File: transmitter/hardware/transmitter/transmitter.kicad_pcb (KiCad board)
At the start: 2 copper layers, 56 x 47 mm, 47 parts, among them J1 SOIL, J2 SOIL, J3 USB_UART, J4 PWR, J5 SOIL, J6 SOIL, J7 SOIL, J8 SOIL, Q1 Si2305CDS, Q2 BSS138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

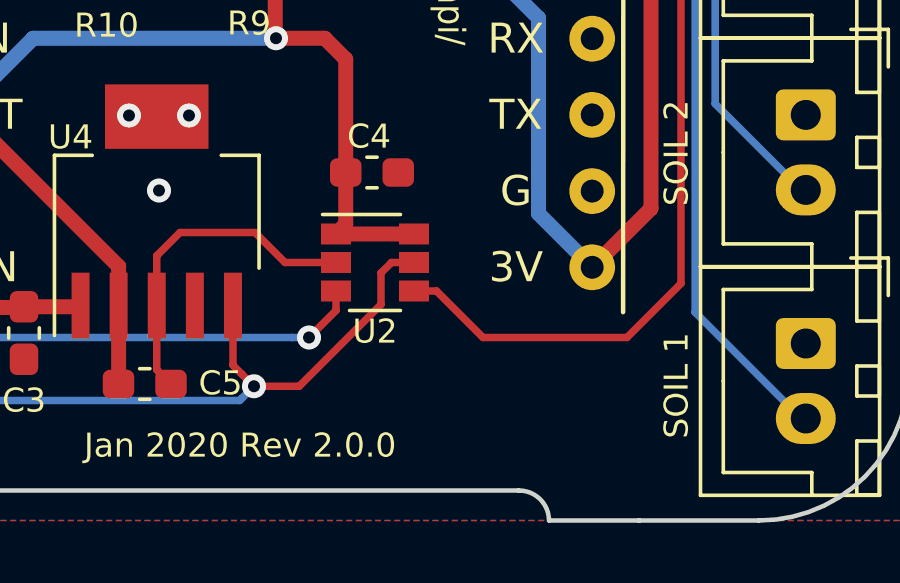
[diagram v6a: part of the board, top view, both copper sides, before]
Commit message: tpl5111 layout tweak
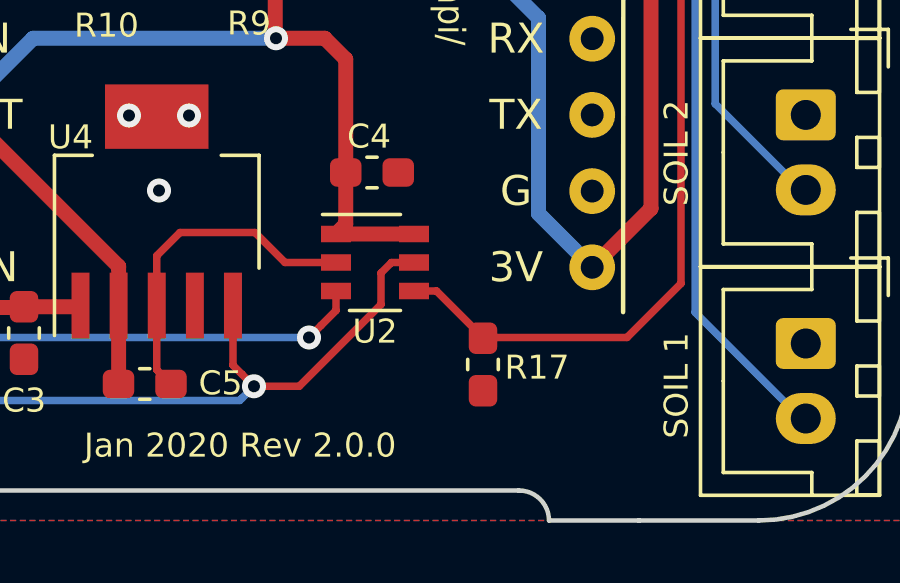
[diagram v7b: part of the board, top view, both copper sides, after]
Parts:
- added R17: 10K, Resistor_SMD:R_0603_1608Metric_Pad1.05x0.95mm_HandSolder, F.Cu at (156.4, 106.7)
- U2: footprint Package_TO_SOT_SMD:SuperSOT-6 -> tpl511x:SOT-6-DDC
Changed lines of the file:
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@@
     (tracks 295)
     (zones 0)
-    (modules 47)
+    (modules 48)
     (nets 28)
   )
@@
     (pad_drill 0.762)
     (pad_to_mask_clearance 0)
+    (solder_mask_min_width 0.25)
     (aux_axis_origin 0 0)
     (grid_origin 134.62 67.945)
@@
     (add_net "Net-(Q3-Pad3)")
   )
+  (module tpl511x:SOT-6-DDC (layer F.Cu)
+    (at 152.82 103.345)
+    (descr "6-pin SuperSOT package http://www.mouser.com/ds/2/149/FMB5551-889214.pdf")
+    (tags "SuperSOT-6 SSOT-6")
+    (attr smd)
+    (fp_text reference U2 (at 0 2.3) (layer F.SilkS)
+      (effects (font (size 0.8 0.8) (thickness 0.15)))
+    )
+    (fp_text value tpl5111 (at 0 2.5) (layer F.Fab)
+      (effects (font (size 1 1) (thickness 0.15)))
+    )
+    (fp_text user %R (at 0 0 90) (layer F.Fab)
+      (effects (font (size 0.5 0.5) (thickness 0.075)))
+    )
+    (fp_line (start 0.85 -1.6) (end -1.75 -1.6) (layer F.SilkS) (width 0.12))
+    (fp_line (start 0.85 1.6) (end -0.85 1.6) (layer F.SilkS) (width 0.12))
+    (fp_line (start -0.85 1.45) (end 0.85 1.45) (layer F.Fab) (width 0.12))
+    (fp_line (start 0.85 1.45) (end 0.85 -1.45) (layer F.Fab) (width 0.12))
+    (fp_line (start 0.85 -1.45) (end -0.4 -1.45) (layer F.Fab) (width 0.12))
+    (fp_line (start -0.4 -1.45) (end -0.85 -1) (layer F.Fab) (width 0.12))
+    (fp_line (start -0.85 -1) (end -0.85 1.45) (layer F.Fab) (width 0.12))
+    (fp_line (start -2.05 -1.7) (end 2.05 -1.7) (layer F.CrtYd) (width 0.05))
+    (fp_line (start -2.05 -1.7) (end -2.05 1.7) (layer F.CrtYd) (width 0.05))
+    (fp_line (start 2.05 1.7) (end 2.05 -1.7) (layer F.CrtYd) (width 0.05))
+    (fp_line (start 2.05 1.7) (end -2.05 1.7) (layer F.CrtYd) (width 0.05))
+    (pad 1 smd rect (at -1.3 -0.95) (size 1 0.55) (layers F.Cu F.Paste F.Mask)
+      (net 15 /VBAT))
+    (pad 2 smd rect (at -1.3 0) (size 1 0.55) (layers F.Cu F.Paste F.Mask)
+      (net 1 GND))
+    (pad 3 smd rect (at -1.3 0.95) (size 1 0.55) (layers F.Cu F.Paste F.Mask)
+      (net 25 "Net-(JP1-Pad2)"))
+    (pad 4 smd rect (at 1.3 0.95) (size 1 0.55) (layers F.Cu F.Paste F.Mask)
+      (net 22 DONE))
+    (pad 6 smd rect (at 1.3 -0.95) (size 1 0.55) (layers F.Cu F.Paste F.Mask)
+      (net 15 /VBAT))
+    (pad 5 smd rect (at 1.3 0) (size 1 0.55) (layers F.Cu F.Paste F.Mask)
+      (net 27 "Net-(TP1-Pad1)"))
+    (model ${KISYS3DMOD}/Package_TO_SOT_SMD.3dshapes/SuperSOT-6.wrl
+      (at (xyz 0 0 0))
+      (scale (xyz 1 1 1))
+      (rotate (xyz 0 0 0))
+    )
+  )
   (module "ESP8266:NodeMCU1.0(12-E)" locked (layer F.Cu)
     (at 148.59 88.9)
@@
     )
   )
-  (module Package_TO_SOT_SMD:SuperSOT-6 (layer F.Cu)
-    (at 152.82 103.345)
-    (descr "6-pin SuperSOT package http://www.mouser.com/ds/2/149/FMB5551-889214.pdf")
-    (tags "SuperSOT-6 SSOT-6")
-    (attr smd)
-    (fp_text reference U2 (at 0 2.3) (layer F.SilkS)
-      (effects (font (size 0.8 0.8) (thickness 0.15)))
-    )
-    (fp_text value tpl5111 (at 0 2.5) (layer F.Fab)
-      (effects (font (size 1 1) (thickness 0.15)))
-    )
-    (fp_text user %R (at 0 0 90) (layer F.Fab)
-      (effects (font (size 0.5 0.5) (thickness 0.075)))
-    )
-    (fp_line (start 0.85 -1.6) (end -1.75 -1.6) (layer F.SilkS) (width 0.12))
-    (fp_line (start 0.85 1.6) (end -0.85 1.6) (layer F.SilkS) (width 0.12))
-    (fp_line (start -0.85 1.45) (end 0.85 1.45) (layer F.Fab) (width 0.12))
-    (fp_line (start 0.85 1.45) (end 0.85 -1.45) (layer F.Fab) (width 0.12))
-    (fp_line (start 0.85 -1.45) (end -0.4 -1.45) (layer F.Fab) (width 0.12))
-    (fp_line (start -0.4 -1.45) (end -0.85 -1) (layer F.Fab) (width 0.12))
-    (fp_line (start -0.85 -1) (end -0.85 1.45) (layer F.Fab) (width 0.12))
-    (fp_line (start -2.05 -1.7) (end 2.05 -1.7) (layer F.CrtYd) (width 0.05))
-    (fp_line (start -2.05 -1.7) (end -2.05 1.7) (layer F.CrtYd) (width 0.05))
-    (fp_line (start 2.05 1.7) (end 2.05 -1.7) (layer F.CrtYd) (width 0.05))
-    (fp_line (start 2.05 1.7) (end -2.05 1.7) (layer F.CrtYd) (width 0.05))
-    (pad 1 smd rect (at -1.3 -0.95) (size 1 0.7) (layers F.Cu F.Paste F.Mask)
-      (net 15 /VBAT))
-    (pad 2 smd rect (at -1.3 0) (size 1 0.7) (layers F.Cu F.Paste F.Mask)
-      (net 1 GND))
-    (pad 3 smd rect (at -1.3 0.95) (size 1 0.7) (layers F.Cu F.Paste F.Mask)
-      (net 25 "Net-(JP1-Pad2)"))
-    (pad 4 smd rect (at 1.3 0.95) (size 1 0.7) (layers F.Cu F.Paste F.Mask)
-      (net 22 DONE))
-    (pad 6 smd rect (at 1.3 -0.95) (size 1 0.7) (layers F.Cu F.Paste F.Mask)
-      (net 15 /VBAT))
-    (pad 5 smd rect (at 1.3 0) (size 1 0.7) (layers F.Cu F.Paste F.Mask)
-      (net 27 "Net-(TP1-Pad1)"))
-    (model ${KISYS3DMOD}/Package_TO_SOT_SMD.3dshapes/SuperSOT-6.wrl
-      (at (xyz 0 0 0))
-      (scale (xyz 1 1 1))
-      (rotate (xyz 0 0 0))
-    )
-  )
   (module Resistor_SMD:R_0603_1608Metric_Pad1.05x0.95mm_HandSolder (layer F.Cu)
     (at 134.62 98.445 90)
@@
       (net 27 "Net-(TP1-Pad1)"))
   )
+  (module Resistor_SMD:R_0603_1608Metric_Pad1.05x0.95mm_HandSolder (layer F.Cu)
+    (at 156.42 106.745 270)
+    (descr "Resistor SMD 0603 (1608 Metric), square (rectangular) end terminal, IPC_7351 nominal with elongated pad for handsoldering. (Body size source: http://www.tortai-tech.com/upload/download/2011102023233369053.pdf), generated with kicad-footprint-generator")
+    (tags "resistor handsolder")
+    (attr smd)
+    (fp_text reference R17 (at 0.1 -1.8) (layer F.SilkS)
+      (effects (font (size 0.8 0.8) (thickness 0.15)))
+    )
+    (fp_text value 10K (at 0 1.43 270) (layer F.Fab)
+      (effects (font (size 1 1) (thickness 0.15)))
+    )
+    (fp_line (start -0.8 0.4) (end -0.8 -0.4) (layer F.Fab) (width 0.1))
+    (fp_line (start -0.8 -0.4) (end 0.8 -0.4) (layer F.Fab) (width 0.1))
+    (fp_line (start 0.8 -0.4) (end 0.8 0.4) (layer F.Fab) (width 0.1))
+    (fp_line (start 0.8 0.4) (end -0.8 0.4) (layer F.Fab) (width 0.1))
+    (fp_line (start -0.171267 -0.51) (end 0.171267 -0.51) (layer F.SilkS) (width 0.12))
+    (fp_line (start -0.171267 0.51) (end 0.171267 0.51) (layer F.SilkS) (width 0.12))
+    (fp_line (start -1.65 0.73) (end -1.65 -0.73) (layer F.CrtYd) (width 0.05))
+    (fp_line (start -1.65 -0.73) (end 1.65 -0.73) (layer F.CrtYd) (width 0.05))
+    (fp_line (start 1.65 -0.73) (end 1.65 0.73) (layer F.CrtYd) (width 0.05))
+    (fp_line (start 1.65 0.73) (end -1.65 0.73) (layer F.CrtYd) (width 0.05))
+    (fp_text user %R (at 0 0 270) (layer F.Fab)
+      (effects (font (size 0.4 0.4) (thickness 0.06)))
+    )
+    (pad 1 smd roundrect (at -0.875 0 270) (size 1.05 0.95) (layers F.Cu F.Paste F.Mask) (roundrect_rratio 0.25)
+      (net 22 DONE))
+    (pad 2 smd roundrect (at 0.875 0 270) (size 1.05 0.95) (layers F.Cu F.Paste F.Mask) (roundrect_rratio 0.25)
+      (net 1 GND))
+    (model ${KISYS3DMOD}/Resistor_SMD.3dshapes/R_0603_1608Metric.wrl
+      (at (xyz 0 0 0))
+      (scale (xyz 1 1 1))
+      (rotate (xyz 0 0 0))
+    )
+  )
   (gr_text TIMER (at 117.42 94.645) (layer F.SilkS)

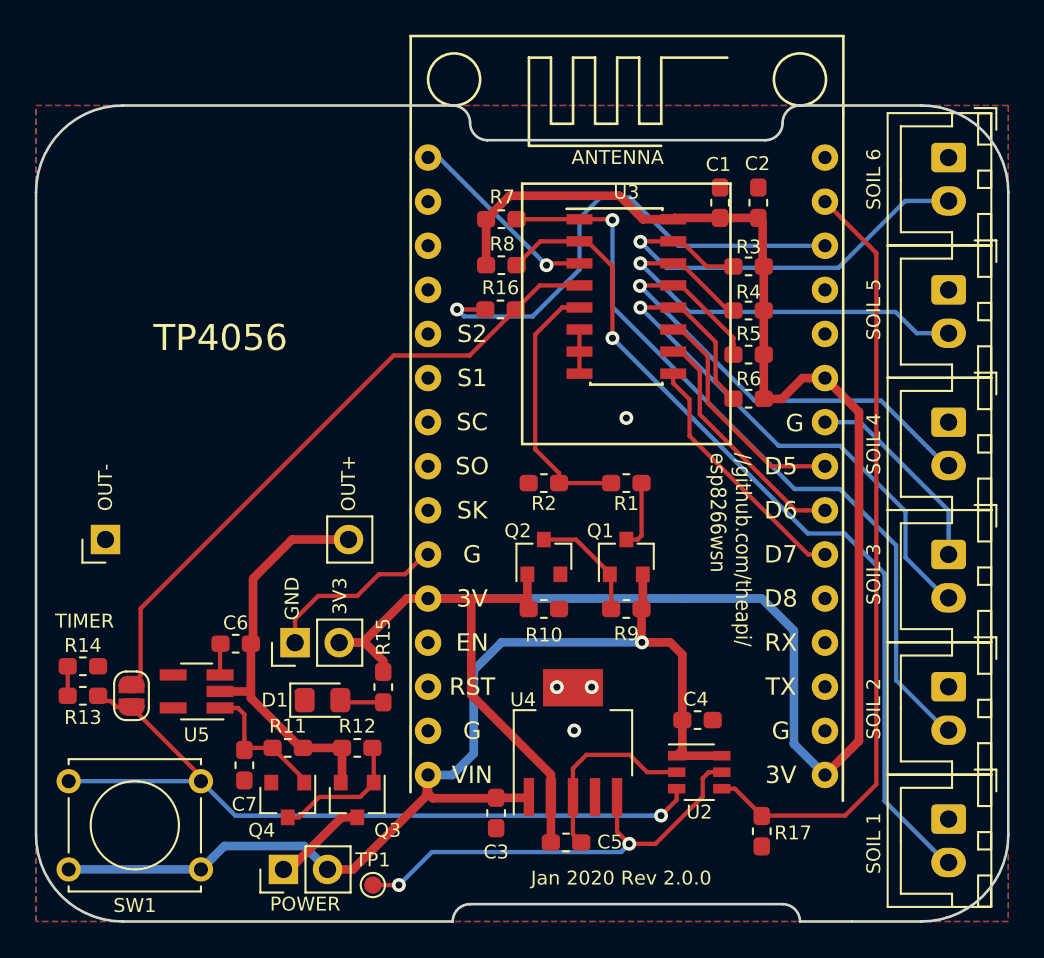
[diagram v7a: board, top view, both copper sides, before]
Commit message: Fit within 70mm circle
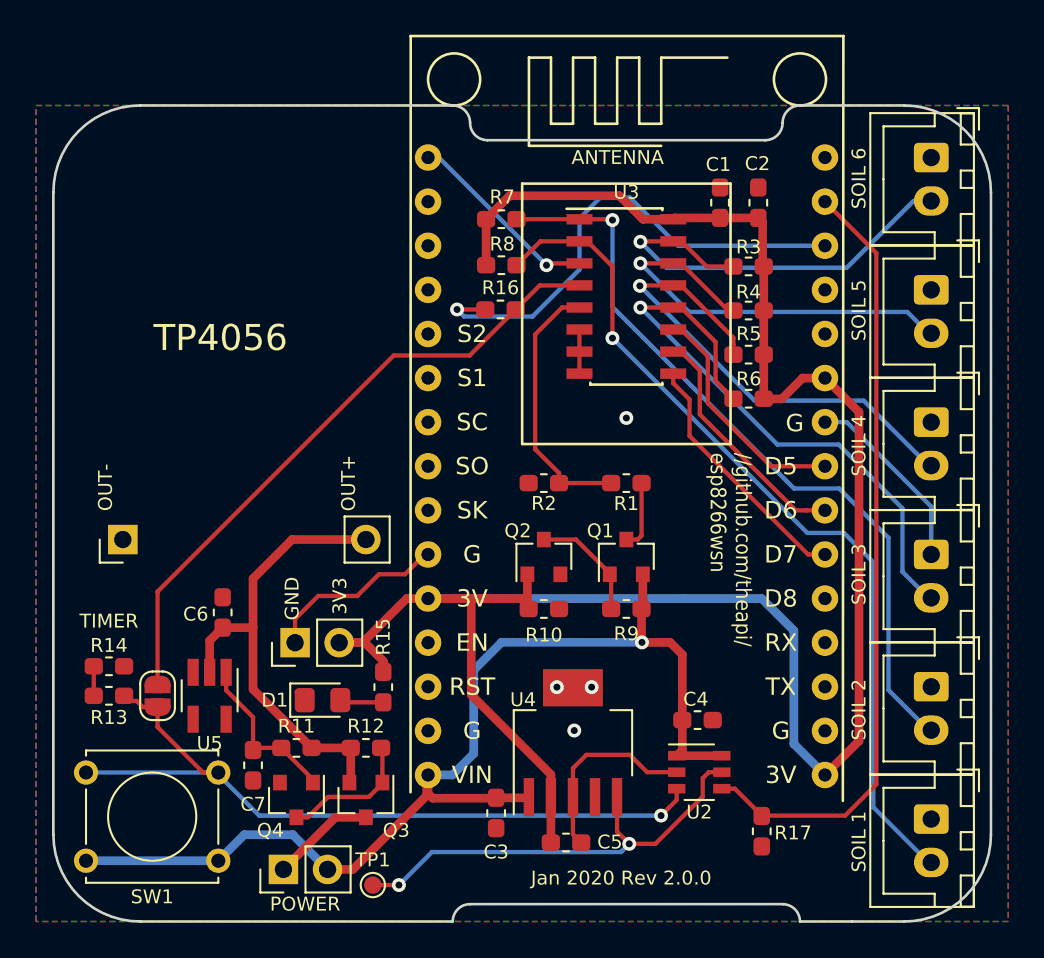
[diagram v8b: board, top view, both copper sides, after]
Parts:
- moved C6 1.95 mm to (125.4, 94.1), turned to 90 degrees
- moved JP1 1.50 mm to (121.6, 98.9)
- moved R13 1.50 mm to (118.8, 98.9)
- moved R14 1.50 mm to (118.8, 97.2)
- moved SW1 1.12 mm to (125.1, 108.4)
- moved J1 1.00 mm to (166.2, 67.9)
- moved J2 1.00 mm to (166.2, 75.6)
- moved J4 1.00 mm to (119.6, 89.9)
- moved J5 1.00 mm to (166.2, 83.2)
- moved J6 1.00 mm to (166.2, 90.8)
- moved J7 1.00 mm to (166.2, 98.4)
- moved J8 1.00 mm to (166.2, 106.0)
- moved U5 0.79 mm to (124.6, 98.9), turned to 270 degrees
- moved C7 0.50 mm to (127.1, 102.9)
- moved Q3 0.50 mm to (133.6, 104.9)
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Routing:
- net /OUT+: track 23.6 -> 27.5 mm
- net GND: track 38.7 -> 35.5 mm
- net Net-(C7-Pad1): track 8.27 -> 9.76 mm
- net SOIL_3: track 29.7 -> 28.7 mm
- net SOIL_2: track 25.9 -> 24.9 mm
- net SOIL_1: track 25.9 -> 24.9 mm
- net Net-(JP1-Pad2): track 44.6 -> 43.7 mm
- net Net-(Q3-Pad3): track 5.49 -> 6.34 mm
- net /VBAT: track 65.3 -> 64.7 mm
- net /DELAY_VAL: track 37.6 -> 37.0 mm
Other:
- board size 56 x 47 mm -> 54 x 47 mm
